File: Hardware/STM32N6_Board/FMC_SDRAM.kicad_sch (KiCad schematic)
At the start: 15 parts

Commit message: Made fixes to remove ERC errors
- 1 remaining error, but > 100 warnings D:
- The remaining error is a bug within KiCAD I believe
- Next is footprint assignment
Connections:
- net FMC_SDNCAS renamed FMC_SKNCAS
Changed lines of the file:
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@@
 		)
 	)
-	(label "FMC_SDNCAS"
+	(label "FMC_SKNCAS"
 		(at 87.63 54.61 270)
 		(effects
@@
 		)
 	)
-	(hierarchical_label "FMC"
+	(hierarchical_label "{FMC}"
 		(shape input)
 		(at 200.66 118.11 0)

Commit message: Completed schematic layout, ERC check, and footprint assignment
- Completed and checked the schematic layout
- Ran the ERC check; no errors (but lots of (checked) warnings)
- Assigned footprints. Most in std lib, others in footprints.pretty
- Imported the components to the PCB Editor, and fixed errors
- All that's left is PCB layout!
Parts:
- removed U11: ~, symbol STM32N6_Symbols:IS42S16800F-7TLI
- added U11: IS42S16800F-7BL, STM32N6_Footprints:IS42S16800F-7BL_BGA54C80P9X9_800X800X120, symbol STM32N6_Symbols:IS42S16800F-7BL
- C55, C56, C57, C58, C59, C60, C61, C62, C63, C64, C65, C66, C67, C68: footprint (none) -> Capacitor_SMD:C_0805_2012Metric_Pad1.18x1.45mm_HandSolder
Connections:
- net FMC_A0: now also U11.H7 (A0)
- net FMC_A1: now also U11.H8 (A1)
- net FMC_A10: now also U11.H9 (A10)
- net FMC_A11: now also U11.G2 (A11)
- net FMC_A2: now also U11.J8 (A2)
- net FMC_A3: now also U11.J7 (A3)
- net FMC_A4: now also U11.J3 (A4)
- net FMC_A5: now also U11.J2 (A5)
- net FMC_A6: now also U11.H3 (A6)
- net FMC_A7: now also U11.H2 (A7)
- net FMC_A8: now also U11.H1 (A8)
- net FMC_A9: now also U11.G3 (A9)
- net FMC_BA0: now also U11.G7 (BA0)
- net FMC_BA1: now also U11.G8 (BA1)
- net FMC_D0: now also U11.A8 (DQ0)
- net FMC_D1: now also U11.B9 (DQ1)
- net FMC_D10: now also U11.D1 (DQ10)
- net FMC_D11: now also U11.C2 (DQ11)
- net FMC_D12: now also U11.C1 (DQ12)
- net FMC_D13: now also U11.B2 (DQ13)
- net FMC_D14: now also U11.B1 (DQ14)
- net FMC_D15: now also U11.A2 (DQ15)
- net FMC_D2: now also U11.B8 (DQ2)
- net FMC_D3: now also U11.C9 (DQ3)
- net FMC_D4: now also U11.C8 (DQ4)
- net FMC_D5: now also U11.D9 (DQ5)
- net FMC_D6: now also U11.D8 (DQ6)
- net FMC_D7: now also U11.E9 (DQ7)
- net FMC_D8: now also U11.E1 (DQ8)
- net FMC_D9: now also U11.D2 (DQ9)
- net FMC_NBL0: now also U11.E8 (DQML)
- net FMC_NBL1: now also U11.F1 (DQMH)
- net FMC_SDCKE0: now also U11.F3 (CKE)
- net FMC_SDCLK: now also U11.F2 (CLK)
- net FMC_SDNE0: now also U11.G9 (~CS)
- net FMC_SDNRAS: now also U11.F8 (~RAS)
- net FMC_SDNWE: now also U11.F9 (~WE)
- net FMC_SKNCAS: now also U11.F7 (~CAS)
- net GND: now also U11.A1 (V_SS), U11.A3 (V_SSQ), U11.B7 (V_SSQ), U11.C3 (V_SSQ), U11.D7 (V_SSQ), U11.E3 (V_SS), U11.J1 (V_SS)
- net VDD3V3: now also U11.A7 (V_DDQ), U11.A9 (V_DD), U11.B3 (V_DDQ), U11.C7 (V_DDQ), U11.D3 (V_DDQ), U11.E7 (V_DD), U11.J9 (V_DD)
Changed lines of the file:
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@@
 			)
 		)
-		(property "Footprint" ""
+		(property "Footprint" "Capacitor_SMD:C_0805_2012Metric_Pad1.18x1.45mm_HandSolder"
 			(at 182.88 100.33 0)
 			(effects
@@
 			)
 		)
-		(property "Footprint" ""
+		(property "Footprint" "Capacitor_SMD:C_0805_2012Metric_Pad1.18x1.45mm_HandSolder"
 			(at 190.5 77.47 0)
 			(effects
@@
 			)
 		)
-		(property "Footprint" ""
+		(property "Footprint" "Capacitor_SMD:C_0805_2012Metric_Pad1.18x1.45mm_HandSolder"
 			(at 198.12 100.33 0)
 			(effects
@@
 			)
 		)
-		(property "Footprint" ""
+		(property "Footprint" "Capacitor_SMD:C_0805_2012Metric_Pad1.18x1.45mm_HandSolder"
 			(at 205.74 77.47 0)
 			(effects
@@
 				(path "/4869b3db-9bd3-4900-9c3c-205f01100fa6/0e02e1f8-d407-46cc-9aff-8c3a7585017c"
 					(reference "C65")
-					(unit 1)
-				)
-			)
-		)
-	)
-	(symbol
-		(lib_id "STM32N6_Symbols:IS42S16800F-7TLI")
-		(at 95.25 96.52 0)
-		(unit 1)
-		(exclude_from_sim no)
-		(in_bom yes)
-		(on_board yes)
-		(dnp no)
-		(fields_autoplaced yes)
-		(property "Reference" "U11"
-			(at 115.1733 67.31 0)
-			(effects
-				(font
-					(size 1.27 1.27)
-				)
-				(justify left)
-			)
-		)
-		(property "Value" "~"
-			(at 115.1733 69.85 0)
-			(effects
-				(font
-					(size 1.27 1.27)
-				)
-				(justify left)
-			)
-		)
-		(property "Footprint" ""
-			(at 95.25 96.52 0)
-			(effects
-				(font
-					(size 1.27 1.27)
-				)
-				(hide yes)
-			)
-		)
-		(property "Datasheet" ""
-			(at 95.25 96.52 0)
-			(effects
-				(font
-					(size 1.27 1.27)
-				)
-				(hide yes)
-			)
-		)
-		(property "Description" ""
-			(at 95.25 96.52 0)
-			(effects
-				(font
-					(size 1.27 1.27)
-				)
-				(hide yes)
-			)
-		)
-		(pin "26"
-		)
-		(pin "19"
-		)
-		(pin "23"
-		)
-		(pin "16"
-		)
-		(pin "35"
-		)
-		(pin "43"
-		)
-		(pin "52"
-		)
-		(pin "25"
-		)
-		(pin "37"
-		)
-		(pin "39"
-		)
-		(pin "9"
-		)
-		(pin "3"
-		)
-		(pin "49"
-		)
-		(pin "22"
-		)
-		(pin "27"
-		)
-		(pin "41"
-		)
-		(pin "24"
-		)
-		(pin "29"
-		)
-		(pin "30"
-		)
-		(pin "31"
-		)
-		(pin "33"
-		)
-		(pin "17"
-		)
-		(pin "32"
-		)
-		(pin "34"
-		)
-		(pin "36"
-		)
-		(pin "15"
-		)
-		(pin "40"
-		)
-		(pin "38"
-		)
-		(pin "18"
-		)
-		(pin "20"
-		)
-		(pin "21"
-		)
-		(pin "6"
-		)
-		(pin "12"
-		)
-		(pin "46"
-		)
-		(pin "1"
-		)
-		(pin "54"
-		)
-		(pin "14"
-		)
-		(pin "28"
-		)
-		(pin "2"
-		)
-		(pin "4"
-		)
-		(pin "5"
-		)
-		(pin "10"
-		)
-		(pin "13"
-		)
-		(pin "42"
-		)
-		(pin "53"
-		)
-		(pin "8"
-		)
-		(pin "51"
-		)
-		(pin "7"
-		)
-		(pin "11"
-		)
-		(pin "50"
-		)
-		(pin "44"
-		)
-		(pin "45"
-		)
-		(pin "47"
-		)
-		(pin "48"
-		)
-		(instances
-			(project ""
-				(path "/4869b3db-9bd3-4900-9c3c-205f01100fa6/0e02e1f8-d407-46cc-9aff-8c3a7585017c"
-					(reference "U11")
 					(unit 1)
 				)
@@
 			)
 		)
-		(property "Footprint" ""
+		(property "Footprint" "Capacitor_SMD:C_0805_2012Metric_Pad1.18x1.45mm_HandSolder"
 			(at 182.88 77.47 0)
 			(effects
@@
 			)
 		)
-		(property "Footprint" ""
+		(property "Footprint" "Capacitor_SMD:C_0805_2012Metric_Pad1.18x1.45mm_HandSolder"
 			(at 190.5 100.33 0)
 			(effects
@@
 			)
 		)
-		(property "Footprint" ""
+		(property "Footprint" "Capacitor_SMD:C_0805_2012Metric_Pad1.18x1.45mm_HandSolder"
 			(at 198.12 77.47 0)
 			(effects
@@
 			)
 		)
-		(property "Footprint" ""
+		(property "Footprint" "Capacitor_SMD:C_0805_2012Metric_Pad1.18x1.45mm_HandSolder"
 			(at 175.26 100.33 0)
 			(effects
@@
 			)
 		)
-		(property "Footprint" ""
+		(property "Footprint" "Capacitor_SMD:C_0805_2012Metric_Pad1.18x1.45mm_HandSolder"
 			(at 205.74 100.33 0)
 			(effects
@@
 			)
 		)
-		(property "Footprint" ""
+		(property "Footprint" "Capacitor_SMD:C_0805_2012Metric_Pad1.18x1.45mm_HandSolder"
 			(at 213.36 100.33 0)
 			(effects
@@
 			)
 		)
-		(property "Footprint" ""
+		(property "Footprint" "Capacitor_SMD:C_0805_2012Metric_Pad1.18x1.45mm_HandSolder"
 			(at 213.36 77.47 0)
 			(effects
@@
 			)
 		)
-		(property "Footprint" ""
+		(property "Footprint" "Capacitor_SMD:C_0805_2012Metric_Pad1.18x1.45mm_HandSolder"
 			(at 175.26 77.47 0)
 			(effects
@@
 			)
 		)
-		(property "Footprint" ""
+		(property "Footprint" "Capacitor_SMD:C_0805_2012Metric_Pad1.18x1.45mm_HandSolder"
 			(at 220.98 77.47 0)
 			(effects
@@
 			)
 		)
-		(property "Footprint" ""
+		(property "Footprint" "Capacitor_SMD:C_0805_2012Metric_Pad1.18x1.45mm_HandSolder"
 			(at 228.6 77.47 0)
 			(effects
@@
 					(unit 1)
 				)
+			)
+		)
+	)
+	(symbol
+		(lib_id "STM32N6_Symbols:IS42S16800F-7BL")
+		(at 95.25 96.52 0)
+		(unit 1)
+		(exclude_from_sim no)
+		(in_bom yes)
+		(on_board yes)
+		(dnp no)
+		(property "Reference" "U11"
+			(at 113.792 67.31 0)
+			(effects
+				(font
+					(size 1.27 1.27)
+				)
+				(justify left)
+			)
+		)
+		(property "Value" "IS42S16800F-7BL"
+			(at 113.792 69.85 0)
+			(effects
+				(font
+					(size 1.27 1.27)
+				)
+				(justify left)
+			)
+		)
+		(property "Footprint" "STM32N6_Footprints:IS42S16800F-7BL_BGA54C80P9X9_800X800X120"
+			(at 95.25 96.52 0)
+			(effects
+				(font
+					(size 1.27 1.27)
+				)
+				(hide yes)
+			)
+		)
+		(property "Datasheet" ""
+			(at 95.25 96.52 0)
+			(effects
+				(font
+					(size 1.27 1.27)
+				)
+				(hide yes)
+			)
+		)
+		(property "Description" ""
+			(at 95.25 96.52 0)
+			(effects
+				(font
+					(size 1.27 1.27)
+				)
+				(hide yes)
+			)
+		)
+		(pin "E2"
+		)
+		(pin "G2"
+		)
+		(pin "F8"
+		)
+		(pin "A7"
+		)
+		(pin "A1"
+		)
+		(pin "H7"
+		)
+		(pin "J3"
+		)
+		(pin "H9"
+		)
+		(pin "F2"
+		)
+		(pin "F9"
+		)
+		(pin "H3"
+		)
+		(pin "B3"
+		)
+		(pin "F1"
+		)
+		(pin "G8"
+		)
+		(pin "F7"
+		)
+		(pin "A3"
+		)
+		(pin "C7"
+		)
+		(pin "D3"
+		)
+		(pin "C8"
+		)
+		(pin "B7"
+		)
+		(pin "E7"
+		)
+		(pin "E1"
+		)
+		(pin "D2"
+		)
+		(pin "D1"
+		)
+		(pin "D7"
+		)
+		(pin "H8"
+		)
+		(pin "A9"
+		)
+		(pin "G3"
+		)
+		(pin "E8"
+		)
+		(pin "J2"
+		)
+		(pin "J8"
+		)
+		(pin "J7"
+		)
+		(pin "H2"
+		)
+		(pin "H1"
+		)
+		(pin "G1"
+		)
+		(pin "F3"
+		)
+		(pin "G9"
+		)
+		(pin "G7"
+		)
+		(pin "C3"
+		)
+		(pin "E3"
+		)
+		(pin "J9"
+		)
+		(pin "J1"
+		)
+		(pin "B9"
+		)
+		(pin "C9"
+		)
+		(pin "D8"
+		)
+		(pin "E9"
+		)
+		(pin "A8"
+		)
+		(pin "B8"
+		)
+		(pin "D9"
+		)
+		(pin "A2"
+		)
+		(pin "C1"
+		)
+		(pin "B2"
+		)
+		(pin "C2"
+		)
+		(pin "B1"
+		)
+		(instances
+			(project ""
+				(path "/4869b3db-9bd3-4900-9c3c-205f01100fa6/0e02e1f8-d407-46cc-9aff-8c3a7585017c"
+					(reference "U11")
+					(unit 1)
+				)

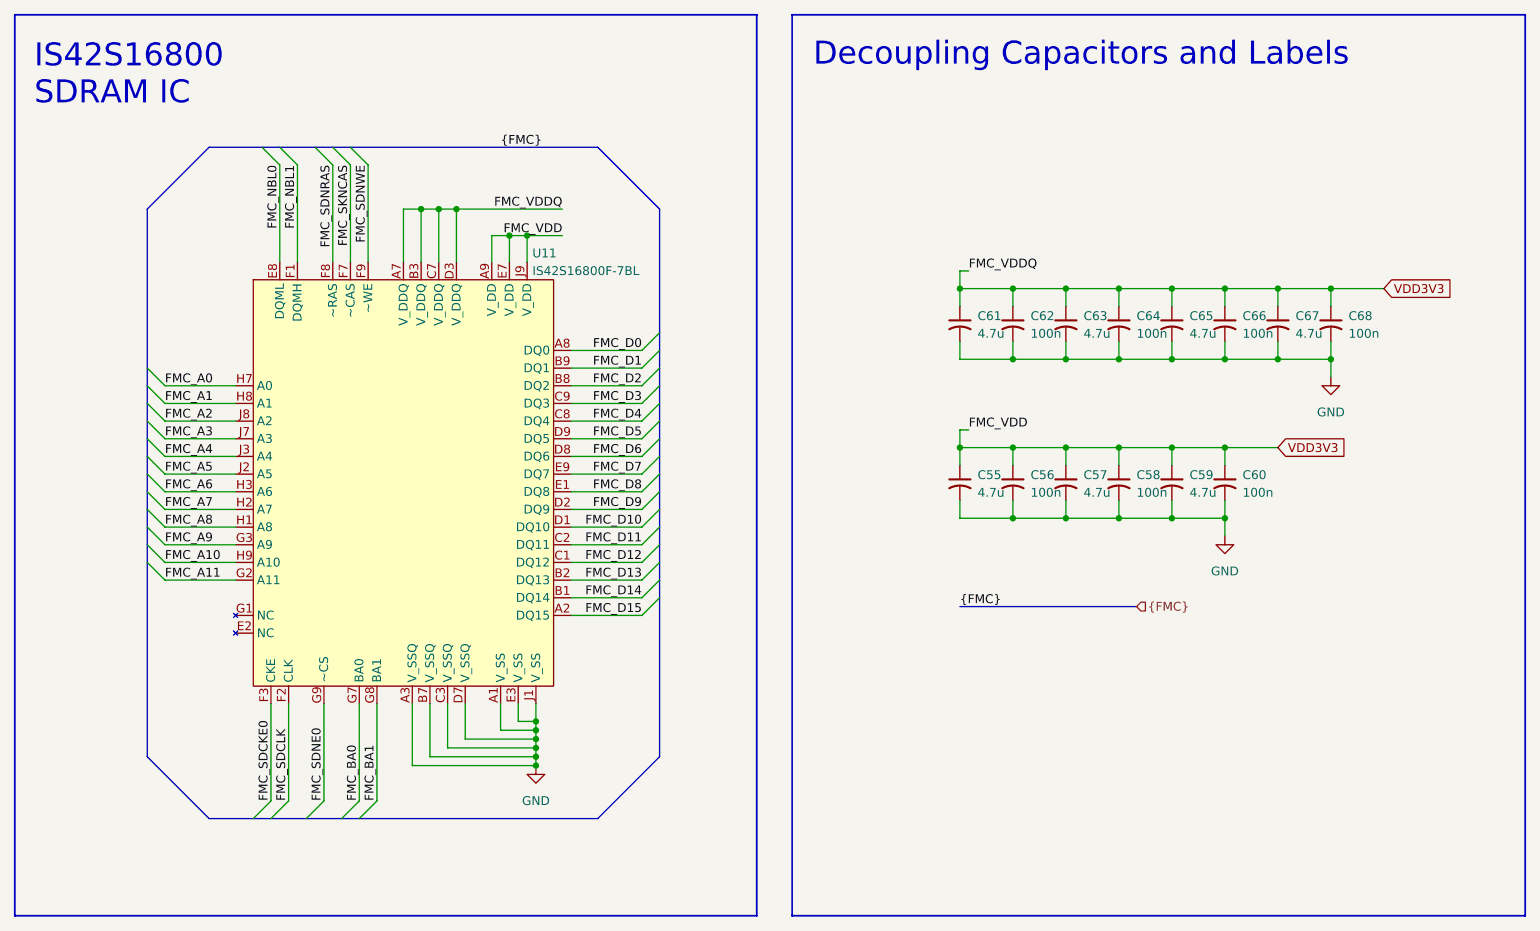
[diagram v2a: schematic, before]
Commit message: Completed a lot of the layout of the STM Board
- Major layout complete, but all the wiring still left. 488 open nets!
- The STM32's BGA fanout is complete, now comes laying out traces
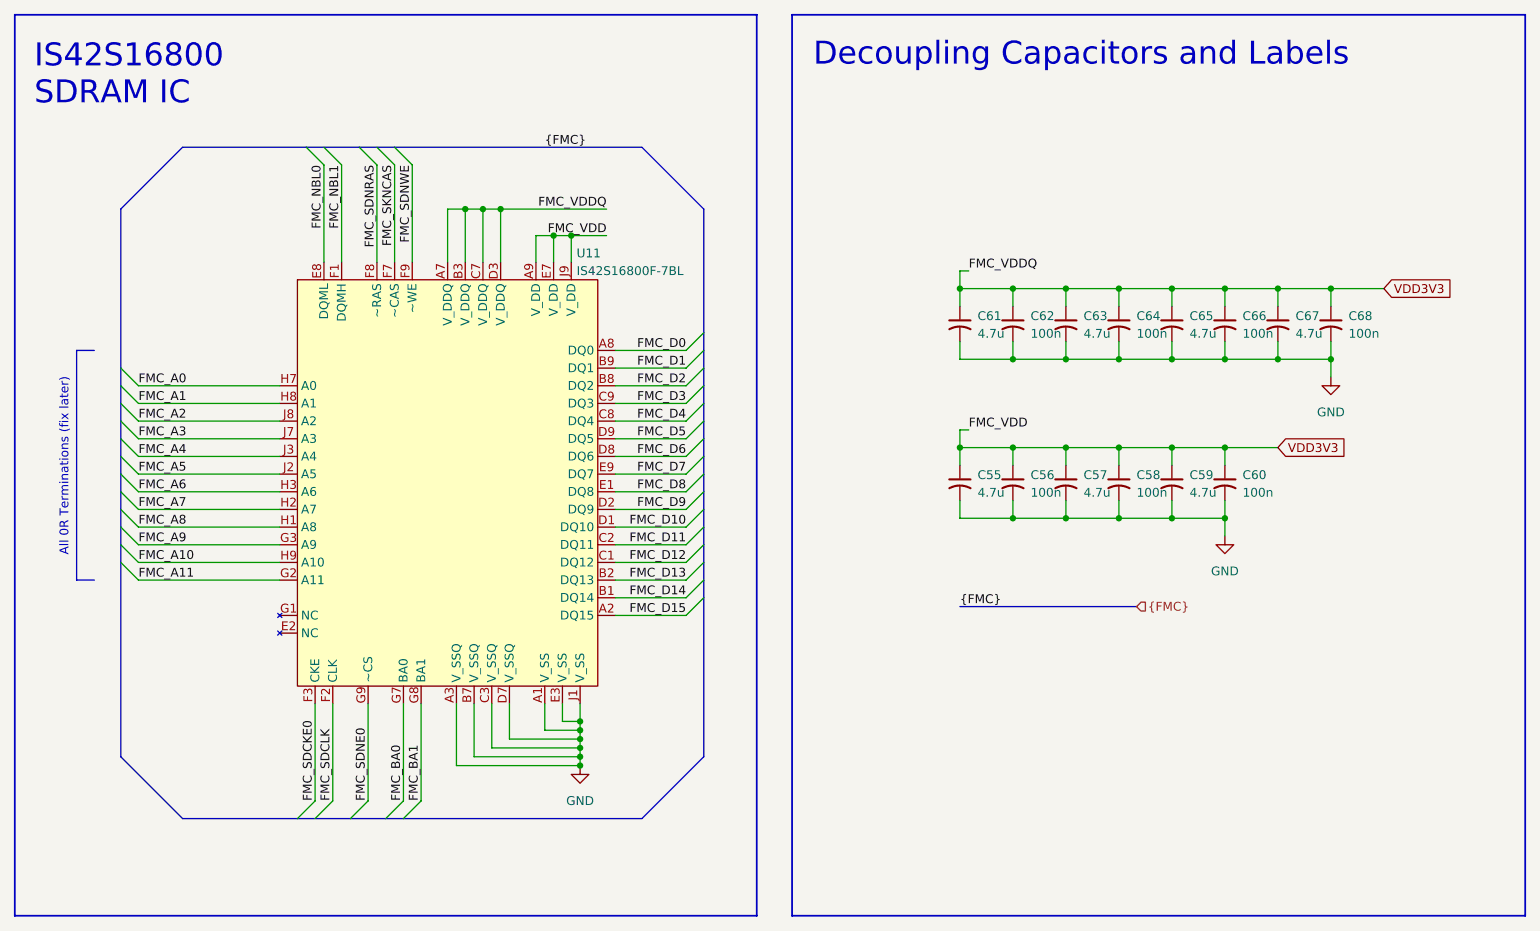
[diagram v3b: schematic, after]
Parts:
- C55, C56, C57, C58, C59, C60, C61, C62, C63, C64, C65, C66, C67, C68: footprint Capacitor_SMD:C_0805_2012Metric_Pad1.18x1.45mm_HandSolder -> Capacitor_SMD:C_0402_1005Metric
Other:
- note added: "All 0R Terminations (fix later)"
- moved on the sheet: U11

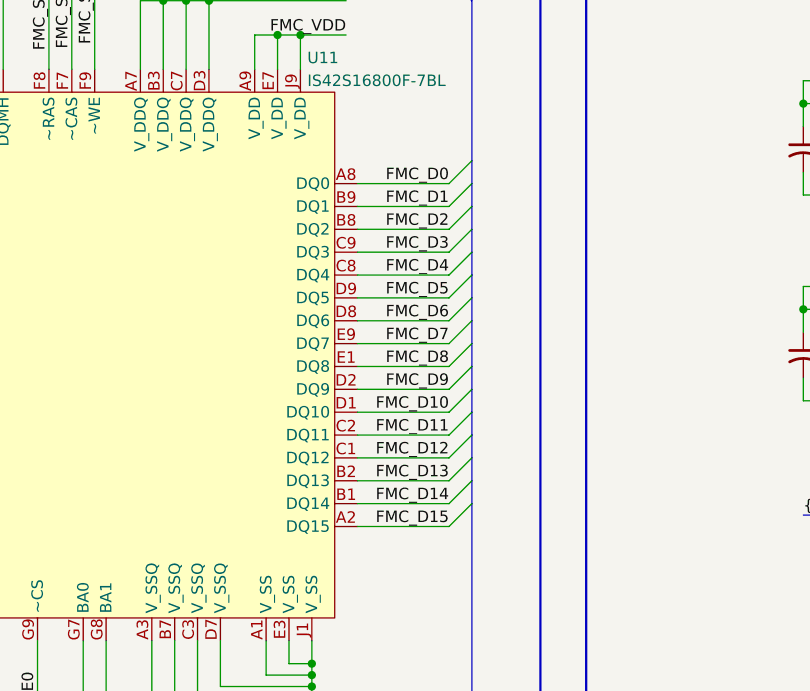
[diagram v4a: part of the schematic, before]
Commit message: Finished the SDRAM wiring
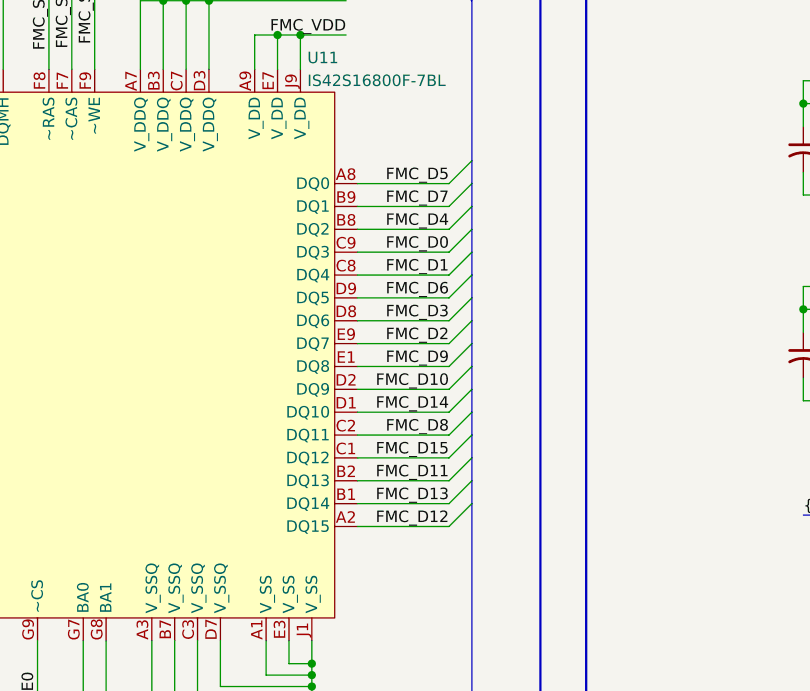
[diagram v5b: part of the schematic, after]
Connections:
- net FMC_D0: now also U11.C9 (DQ3); no longer U11.A8 (DQ0)
- net FMC_D1: now also U11.C8 (DQ4); no longer U11.B9 (DQ1)
- net FMC_D10: now also U11.D2 (DQ9); no longer U11.D1 (DQ10)
- net FMC_D11: now also U11.B2 (DQ13); no longer U11.C2 (DQ11)
- net FMC_D12: now also U11.A2 (DQ15); no longer U11.C1 (DQ12)
- net FMC_D13: now also U11.B1 (DQ14); no longer U11.B2 (DQ13)
- net FMC_D14: now also U11.D1 (DQ10); no longer U11.B1 (DQ14)
- net FMC_D15: now also U11.C1 (DQ12); no longer U11.A2 (DQ15)
- net FMC_D2: now also U11.E9 (DQ7); no longer U11.B8 (DQ2)
- net FMC_D3: now also U11.D8 (DQ6); no longer U11.C9 (DQ3)
- net FMC_D4: now also U11.B8 (DQ2); no longer U11.C8 (DQ4)
- net FMC_D5: now also U11.A8 (DQ0); no longer U11.D9 (DQ5)
- net FMC_D6: now also U11.D9 (DQ5); no longer U11.D8 (DQ6)
- net FMC_D7: now also U11.B9 (DQ1); no longer U11.E9 (DQ7)
- net FMC_D8: now also U11.C2 (DQ11); no longer U11.E1 (DQ8)
- net FMC_D9: now also U11.E1 (DQ8); no longer U11.D2 (DQ9)
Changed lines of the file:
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@@
 	)
 	(label "FMC_D1"
-		(at 135.89 83.82 180)
+		(at 135.89 91.44 180)
 		(effects
 			(font
@@
 	)
 	(label "FMC_D2"
-		(at 135.89 86.36 180)
+		(at 135.89 99.06 180)
 		(effects
 			(font
@@
 	)
 	(label "FMC_D11"
-		(at 135.89 109.22 180)
+		(at 135.89 114.3 180)
 		(effects
 			(font
@@
 	)
 	(label "FMC_D12"
-		(at 135.89 111.76 180)
+		(at 135.89 119.38 180)
 		(effects
 			(font
@@
 	)
 	(label "FMC_D3"
-		(at 135.89 88.9 180)
+		(at 135.89 96.52 180)
 		(effects
 			(font
@@
 	)
 	(label "FMC_D13"
-		(at 135.89 114.3 180)
+		(at 135.89 116.84 180)
 		(effects
 			(font
@@
 	)
 	(label "FMC_D0"
-		(at 135.89 81.28 180)
+		(at 135.89 88.9 180)
 		(effects
 			(font
@@
 	)
 	(label "FMC_D8"
-		(at 135.89 101.6 180)
+		(at 135.89 109.22 180)
 		(effects
 			(font
@@
 	)
 	(label "FMC_D14"
-		(at 135.89 116.84 180)
+		(at 135.89 106.68 180)
 		(effects
 			(font
@@
 	)
 	(label "FMC_D9"
-		(at 135.89 104.14 180)
+		(at 135.89 101.6 180)
 		(effects
 			(font
@@
 	)
 	(label "FMC_D10"
-		(at 135.89 106.68 180)
+		(at 135.89 104.14 180)
 		(effects
 			(font
@@
 	)
 	(label "FMC_D4"
-		(at 135.89 91.44 180)
+		(at 135.89 86.36 180)
 		(effects
 			(font
@@
 	)
 	(label "FMC_D6"
-		(at 135.89 96.52 180)
+		(at 135.89 93.98 180)
 		(effects
 			(font
@@
 	)
 	(label "FMC_D15"
-		(at 135.89 119.38 180)
+		(at 135.89 111.76 180)
 		(effects
 			(font
@@
 	)
 	(label "FMC_D5"
-		(at 135.89 93.98 180)
+		(at 135.89 81.28 180)
 		(effects
 			(font
@@
 	)
 	(label "FMC_D7"
-		(at 135.89 99.06 180)
-		(effects
-			(font
+		(at 135.89 83.82 180)
+		(effects
+			(font
